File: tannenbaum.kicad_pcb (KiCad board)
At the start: 2 copper layers, 228 x 153 mm, 43 parts, among them Q1 MMBT3904-7-F, Q2 MMBT3904-7-F, Q3 MMBT3904-7-F, Q4 MMBT3904-7-F, Q5 2N7002, Q6 BSS84, SW1 SW_SPDT, U1 ICM7555IPAZ, U2 AP7380-33Y-13, U2 LP2985-3.3

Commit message: pcb
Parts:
- added U1: ICM7555xB, Package_SO:SOIC-8_3.9x4.9mm_P1.27mm, F.Cu at (46.3, 174.0)
- moved D4 59.3 mm to (84.2, 121.3)
- moved D8 55.7 mm to (83.5, 114.9)
- moved D12 54.3 mm to (84.8, 109.9)
- moved R9 5.45 mm to (29.2, 127.6)
- moved R10 2.04 mm to (29.5, 134.0)
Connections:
- C2 pad 1: Net-(U1-CONT) -> Net-(U1-CV)
- R12 pad 1: Net-(U1-OUT) -> /CMD
- R12 pad 2: /CMD -> Net-(U1-Q)
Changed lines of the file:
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@@
   (net 32 "unconnected-(SW1-A-Pad1)")
   (net 33 "/{slash}CMD")
+  (net 34 "Net-(U1-CV)")
+  (net 35 "Net-(U1-Q)")
   (footprint "Capacitor_SMD:C_0805_2012Metric" (layer "F.Cu")
     (at 66.36 123.825)
@@
   (footprint "digikey-footprints:Switch_Slide_JS202011SCQN" (layer "F.Cu")
     (at 21.775 108.125)
-    (property "Purpose" "")
+    (property "Purpose" "On - Off")
     (property "Sheetfile" "psu.kicad_sch")
     (property "Sheetname" "PSU")
@@
   )
   (footprint "LED_SMD:LED_0805_2012Metric" (layer "F.Cu")
-    (at 25.515 130.085)
+    (at 84.1525 121.285)
     (descr "LED SMD 0805 (2012 Metric), square (rectangular) end terminal, IPC_7351 nominal, (Body size source: https://docs.google.com/spreadsheets/d/1BsfQQcO9C6DZCsRaXUlFlo91Tg2WpOkGARC1WS5S8t0/edit?usp=sharing), generated with kicad-footprint-generator")
     (tags "LED")
@@
   )
   (footprint "LED_SMD:LED_0805_2012Metric" (layer "F.Cu")
-    (at 34.415 130.085)
+    (at 84.7875 109.855)
     (descr "LED SMD 0805 (2012 Metric), square (rectangular) end terminal, IPC_7351 nominal, (Body size source: https://docs.google.com/spreadsheets/d/1BsfQQcO9C6DZCsRaXUlFlo91Tg2WpOkGARC1WS5S8t0/edit?usp=sharing), generated with kicad-footprint-generator")
     (tags "LED")
@@
   )
   (footprint "LED_SMD:LED_0805_2012Metric" (layer "F.Cu")
-    (at 29.965 130.085)
+    (at 83.5175 114.935)
     (descr "LED SMD 0805 (2012 Metric), square (rectangular) end terminal, IPC_7351 nominal, (Body size source: https://docs.google.com/spreadsheets/d/1BsfQQcO9C6DZCsRaXUlFlo91Tg2WpOkGARC1WS5S8t0/edit?usp=sharing), generated with kicad-footprint-generator")
     (tags "LED")
@@
       (stroke (width 0.1) (type solid)) (layer "F.Fab"))
     (pad "1" smd roundrect (at -0.775 0) (size 0.9 0.95) (layers "F.Cu" "F.Paste" "F.Mask") (roundrect_rratio 0.25)
-      (net 4 "Net-(U1-CONT)") (pintype "passive"))
+      (net 34 "Net-(U1-CV)") (pintype "passive"))
     (pad "2" smd roundrect (at 0.775 0) (size 0.9 0.95) (layers "F.Cu" "F.Paste" "F.Mask") (roundrect_rratio 0.25)
       (net 2 "GND") (pintype "passive"))
@@
       (net 13 "/B1 2-3") (pinfunction "A") (pintype "passive"))
     (model "${KICAD6_3DMODEL_DIR}/LED_SMD.3dshapes/LED_0805_2012Metric.wrl"
+      (offset (xyz 0 0 0))
+      (scale (xyz 1 1 1))
+      (rotate (xyz 0 0 0))
+    )
+  )
+  (footprint "Package_SO:SOIC-8_3.9x4.9mm_P1.27mm" (layer "F.Cu")
+    (at 46.29 173.99)
+    (descr "SOIC, 8 Pin (JEDEC MS-012AA, https://www.analog.com/media/en/package-pcb-resources/package/pkg_pdf/soic_narrow-r/r_8.pdf), generated with kicad-footprint-generator ipc_gullwing_generator.py")
+    (tags "SOIC SO")
+    (property "Purpose" "Astable multivibrator")
+    (property "Sheetfile" "tannenbaum.kicad_sch")
+    (property "Sheetname" "")
+    (property "ki_description" "CMOS General Purpose Timer, 555 compatible, SOIC-8")
+    (property "ki_keywords" "single timer 555")
+    (attr smd)
+    (fp_text reference "U1" (at 0 -3.4) (layer "F.SilkS")
+        (effects (font (size 1 1) (thickness 0.15)))
+    )
+    (fp_text value "ICM7555xB" (at 0 3.4) (layer "F.Fab")
+        (effects (font (size 1 1) (thickness 0.15)))
+    )
+    (fp_text user "${REFERENCE}" (at 0 0) (layer "F.Fab")
+        (effects (font (size 0.98 0.98) (thickness 0.15)))
+    )
+    (fp_line (start 0 -2.56) (end -3.45 -2.56)
+      (stroke (width 0.12) (type solid)) (layer "F.SilkS"))
+    (fp_line (start 0 -2.56) (end 1.95 -2.56)
+      (stroke (width 0.12) (type solid)) (layer "F.SilkS"))
+    (fp_line (start 0 2.56) (end -1.95 2.56)
+      (stroke (width 0.12) (type solid)) (layer "F.SilkS"))
+    (fp_line (start 0 2.56) (end 1.95 2.56)
+      (stroke (width 0.12) (type solid)) (layer "F.SilkS"))
+    (fp_line (start -3.7 -2.7) (end -3.7 2.7)
+      (stroke (width 0.05) (type solid)) (layer "F.CrtYd"))
+    (fp_line (start -3.7 2.7) (end 3.7 2.7)
+      (stroke (width 0.05) (type solid)) (layer "F.CrtYd"))
+    (fp_line (start 3.7 -2.7) (end -3.7 -2.7)
+      (stroke (width 0.05) (type solid)) (layer "F.CrtYd"))
+    (fp_line (start 3.7 2.7) (end 3.7 -2.7)
+      (stroke (width 0.05) (type solid)) (layer "F.CrtYd"))
+    (fp_line (start -1.95 -1.475) (end -0.975 -2.45)
+      (stroke (width 0.1) (type solid)) (layer "F.Fab"))
+    (fp_line (start -1.95 2.45) (end -1.95 -1.475)
+      (stroke (width 0.1) (type solid)) (layer "F.Fab"))
+    (fp_line (start -0.975 -2.45) (end 1.95 -2.45)
+      (stroke (width 0.1) (type solid)) (layer "F.Fab"))
+    (fp_line (start 1.95 -2.45) (end 1.95 2.45)
+      (stroke (width 0.1) (type solid)) (layer "F.Fab"))
+    (fp_line (start 1.95 2.45) (end -1.95 2.45)
+      (stroke (width 0.1) (type solid)) (layer "F.Fab"))
+    (pad "1" smd roundrect (at -2.475 -1.905) (size 1.95 0.6) (layers "F.Cu" "F.Paste" "F.Mask") (roundrect_rratio 0.25)
+      (net 2 "GND") (pinfunction "GND") (pintype "power_in"))
+    (pad "2" smd roundrect (at -2.475 -0.635) (size 1.95 0.6) (layers "F.Cu" "F.Paste" "F.Mask") (roundrect_rratio 0.25)
+      (net 5 "/THR") (pinfunction "TR") (pintype "input"))
+    (pad "3" smd roundrect (at -2.475 0.635) (size 1.95 0.6) (layers "F.Cu" "F.Paste" "F.Mask") (roundrect_rratio 0.25)
+      (net 35 "Net-(U1-Q)") (pinfunction "Q") (pintype "output"))
+    (pad "4" smd roundrect (at -2.475 1.905) (size 1.95 0.6) (layers "F.Cu" "F.Paste" "F.Mask") (roundrect_rratio 0.25)
+      (net 3 "/3V3") (pinfunction "R") (pintype "input"))
+    (pad "5" smd roundrect (at 2.475 1.905) (size 1.95 0.6) (layers "F.Cu" "F.Paste" "F.Mask") (roundrect_rratio 0.25)
+      (net 34 "Net-(U1-CV)") (pinfunction "CV") (pintype "input"))
+    (pad "6" smd roundrect (at 2.475 0.635) (size 1.95 0.6) (layers "F.Cu" "F.Paste" "F.Mask") (roundrect_rratio 0.25)
+      (net 5 "/THR") (pinfunction "THR") (pintype "input"))
+    (pad "7" smd roundrect (at 2.475 -0.635) (size 1.95 0.6) (layers "F.Cu" "F.Paste" "F.Mask") (roundrect_rratio 0.25)
+      (net 19 "/DSC") (pinfunction "DIS") (pintype "input"))
+    (pad "8" smd roundrect (at 2.475 -1.905) (size 1.95 0.6) (layers "F.Cu" "F.Paste" "F.Mask") (roundrect_rratio 0.25)
+      (net 3 "/3V3") (pinfunction "VCC") (pintype "power_in"))
+    (model "${KICAD6_3DMODEL_DIR}/Package_SO.3dshapes/SOIC-8_3.9x4.9mm_P1.27mm.wrl"
       (offset (xyz 0 0 0))
       (scale (xyz 1 1 1))
@@
   )
   (footprint "Resistor_SMD:R_0805_2012Metric" (layer "F.Cu")
-    (at 29.485 136.03)
+    (at 29.485 133.985)
     (descr "Resistor SMD 0805 (2012 Metric), square (rectangular) end terminal, IPC_7351 nominal, (Body size source: IPC-SM-782 page 72, https://www.pcb-3d.com/wordpress/wp-content/uploads/ipc-sm-782a_amendment_1_and_2.pdf), generated with kicad-footprint-generator")
     (tags "resistor")
@@
   )
   (footprint "Resistor_SMD:R_0805_2012Metric" (layer "F.Cu")
-    (at 29.485 133.08)
+    (at 29.21 127.635)
     (descr "Resistor SMD 0805 (2012 Metric), square (rectangular) end terminal, IPC_7351 nominal, (Body size source: IPC-SM-782 page 72, https://www.pcb-3d.com/wordpress/wp-content/uploads/ipc-sm-782a_amendment_1_and_2.pdf), generated with kicad-footprint-generator")
     (tags "resistor")
@@
       (stroke (width 0.1) (type solid)) (layer "F.Fab"))
     (pad "1" smd roundrect (at -0.9125 0) (size 1.025 1.4) (layers "F.Cu" "F.Paste" "F.Mask") (roundrect_rratio 0.243902)
-      (net 31 "Net-(U1-OUT)") (pintype "passive"))
+      (net 21 "/CMD") (pintype "passive"))
     (pad "2" smd roundrect (at 0.9125 0) (size 1.025 1.4) (layers "F.Cu" "F.Paste" "F.Mask") (roundrect_rratio 0.243902)
-      (net 21 "/CMD") (pintype "passive"))
+      (net 35 "Net-(U1-Q)") (pintype "passive"))
     (model "${KICAD6_3DMODEL_DIR}/Resistor_SMD.3dshapes/R_0805_2012Metric.wrl"
       (offset (xyz 0 0 0))

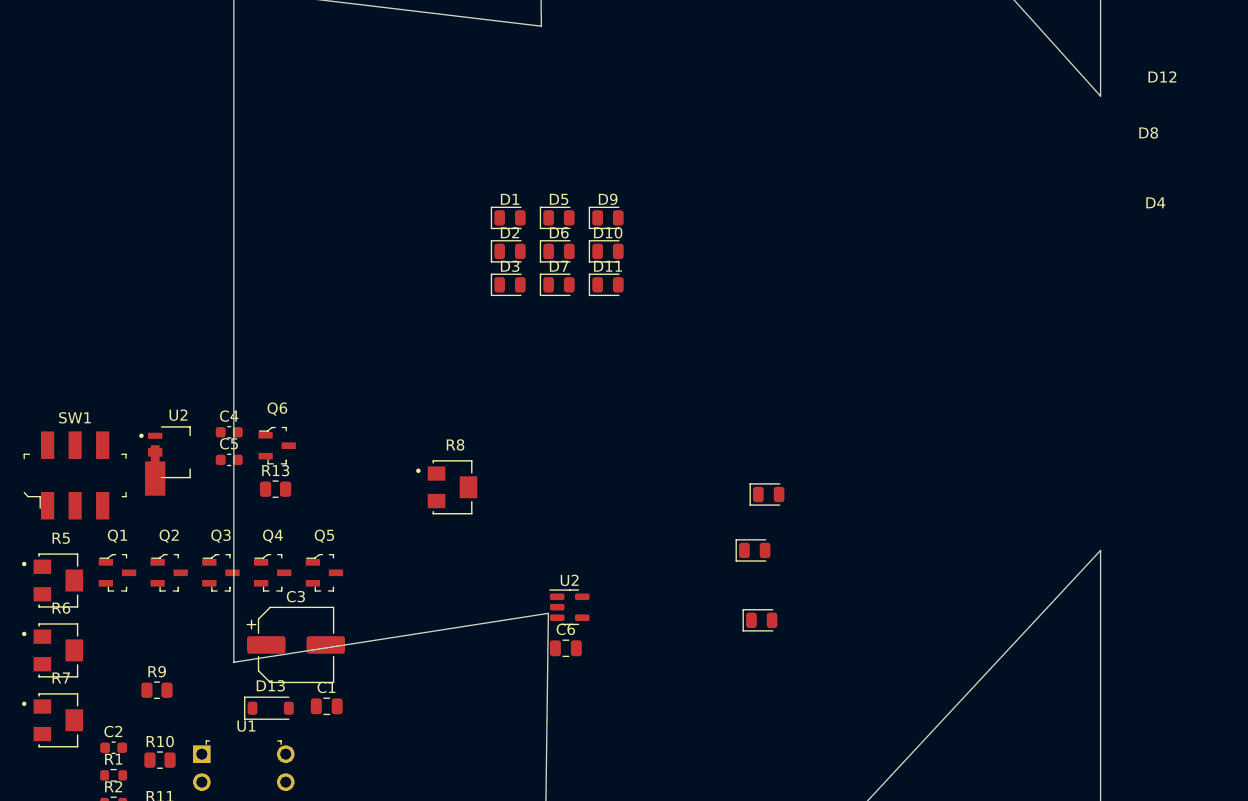
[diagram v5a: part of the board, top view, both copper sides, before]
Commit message: corretti simboli
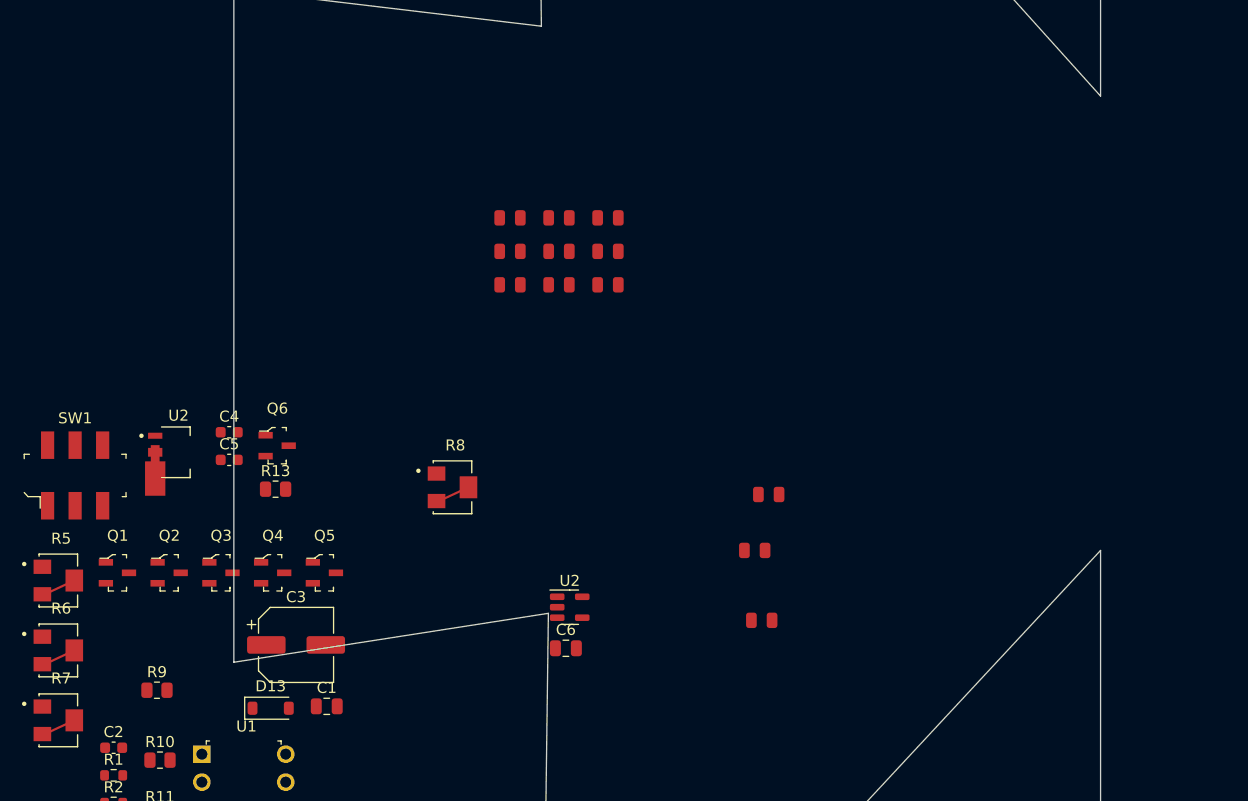
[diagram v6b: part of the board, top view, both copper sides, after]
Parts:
- D1, D10, D11, D12, D2, D3, D4, D5, D6, D7, D8, D9: footprint LED_SMD:LED_0805_2012Metric -> LED_SMD:LED_0805_2012Metric_LW
- R5, R6, R7, R8: footprint PVG5A202C03R00:TRIM_PVG5A202C03R00 -> PVG5A202C03R00:TRIM_PVG5A202C03R00_TWO
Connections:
- R5 pad 3: (no net) -> unconnected-(R5-Pad3)
- R6 pad 3: (no net) -> unconnected-(R6-Pad3)
- R7 pad 3: (no net) -> unconnected-(R7-Pad3)
- R8 pad 3: (no net) -> unconnected-(R8-Pad3)

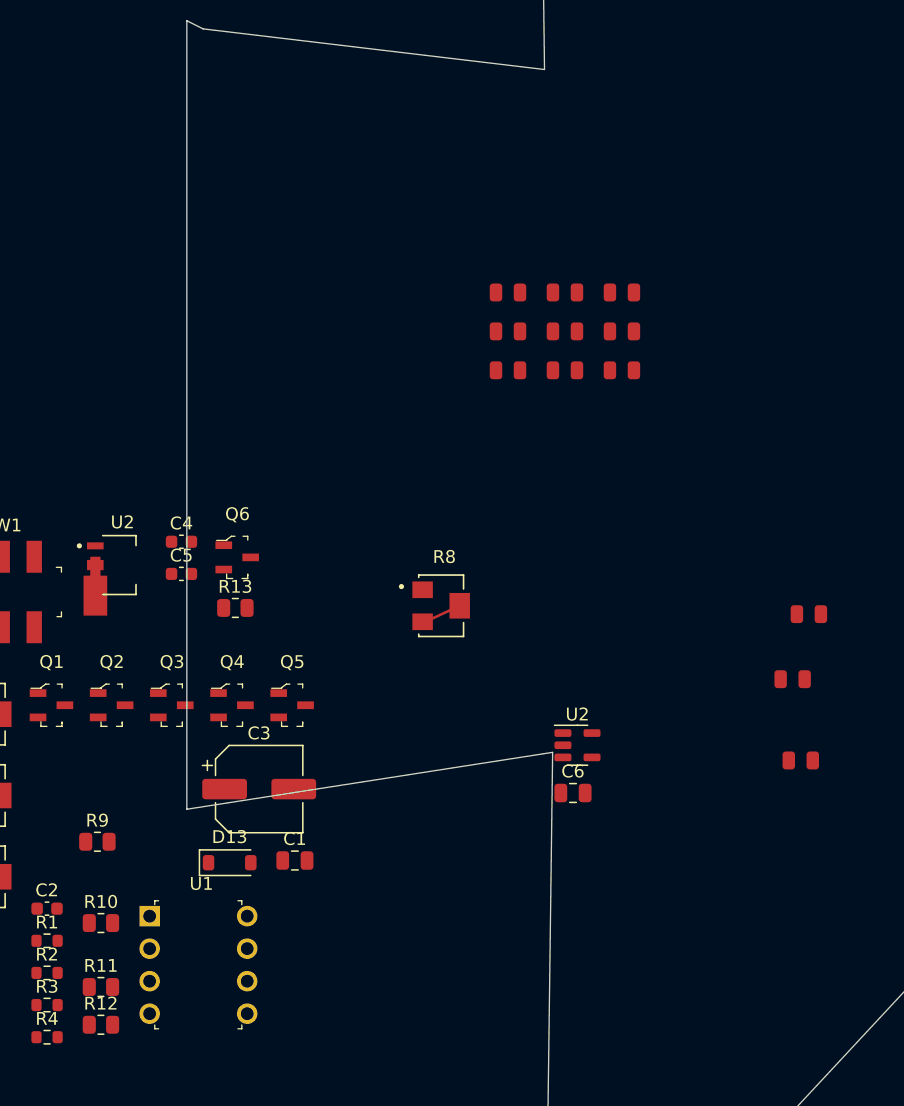
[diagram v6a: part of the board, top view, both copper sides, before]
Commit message: corretti impronte
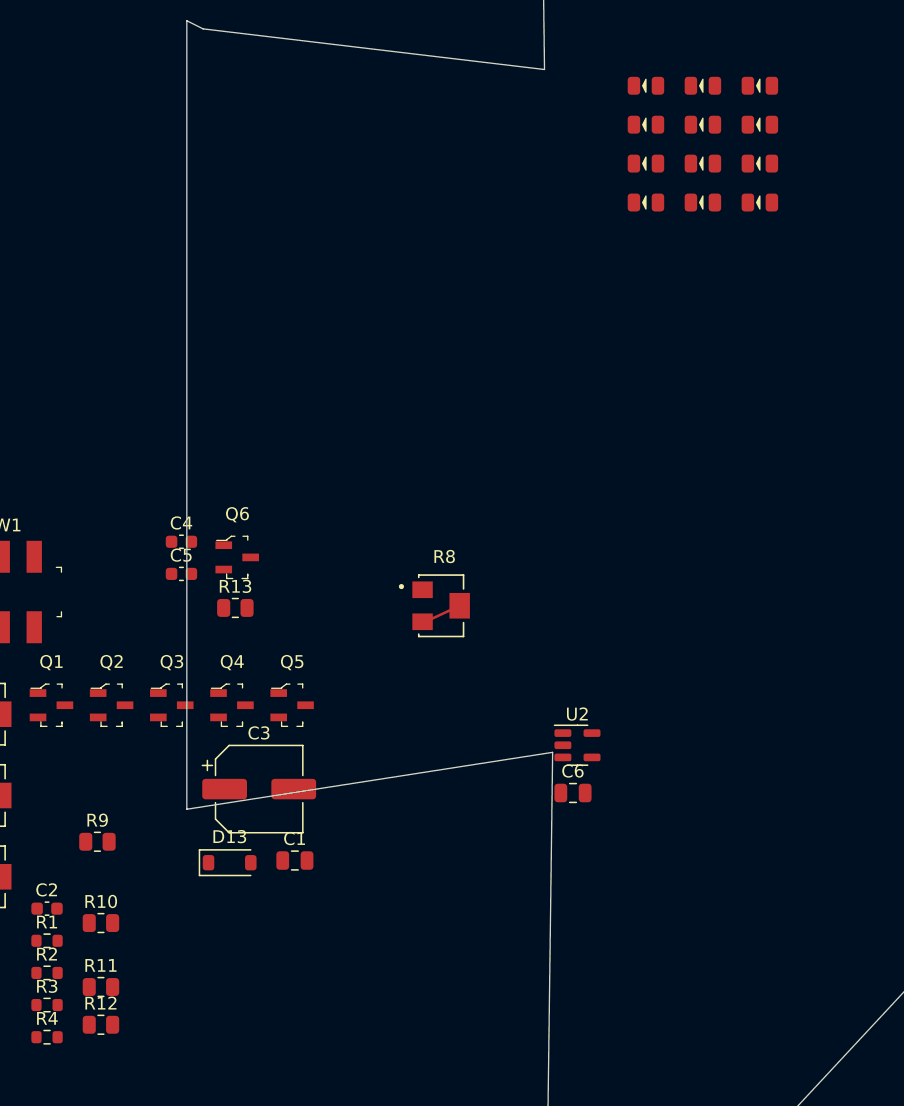
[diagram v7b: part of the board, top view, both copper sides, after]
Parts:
- removed the U1 at (33.3, 133.4)
- removed the U2 at (30.7, 106.0)
- moved D4 45.2 mm to (72.1, 77.7)
- moved D8 37.9 mm to (76.5, 77.7)
- moved D12 32.4 mm to (81.0, 77.7)
- moved D3 19.4 mm to (72.1, 74.7)
- moved D11 19.4 mm to (81.0, 74.7)
- moved D7 19.4 mm to (76.5, 74.7)
- moved D1 19.4 mm to (72.1, 68.6)
- moved D2 19.4 mm to (72.1, 71.6)
- moved D10 19.4 mm to (81.0, 71.6)
- moved D5 19.4 mm to (76.5, 68.6)
- moved D6 19.4 mm to (76.5, 71.6)
- moved D9 19.4 mm to (81.0, 68.6)
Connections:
- R5 pad 3: unconnected-(R5-Pad3) -> GND
- R6 pad 3: unconnected-(R6-Pad3) -> GND
- R7 pad 3: unconnected-(R7-Pad3) -> GND
- R8 pad 3: unconnected-(R8-Pad3) -> GND
